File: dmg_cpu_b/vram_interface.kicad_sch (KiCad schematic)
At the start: 177 parts

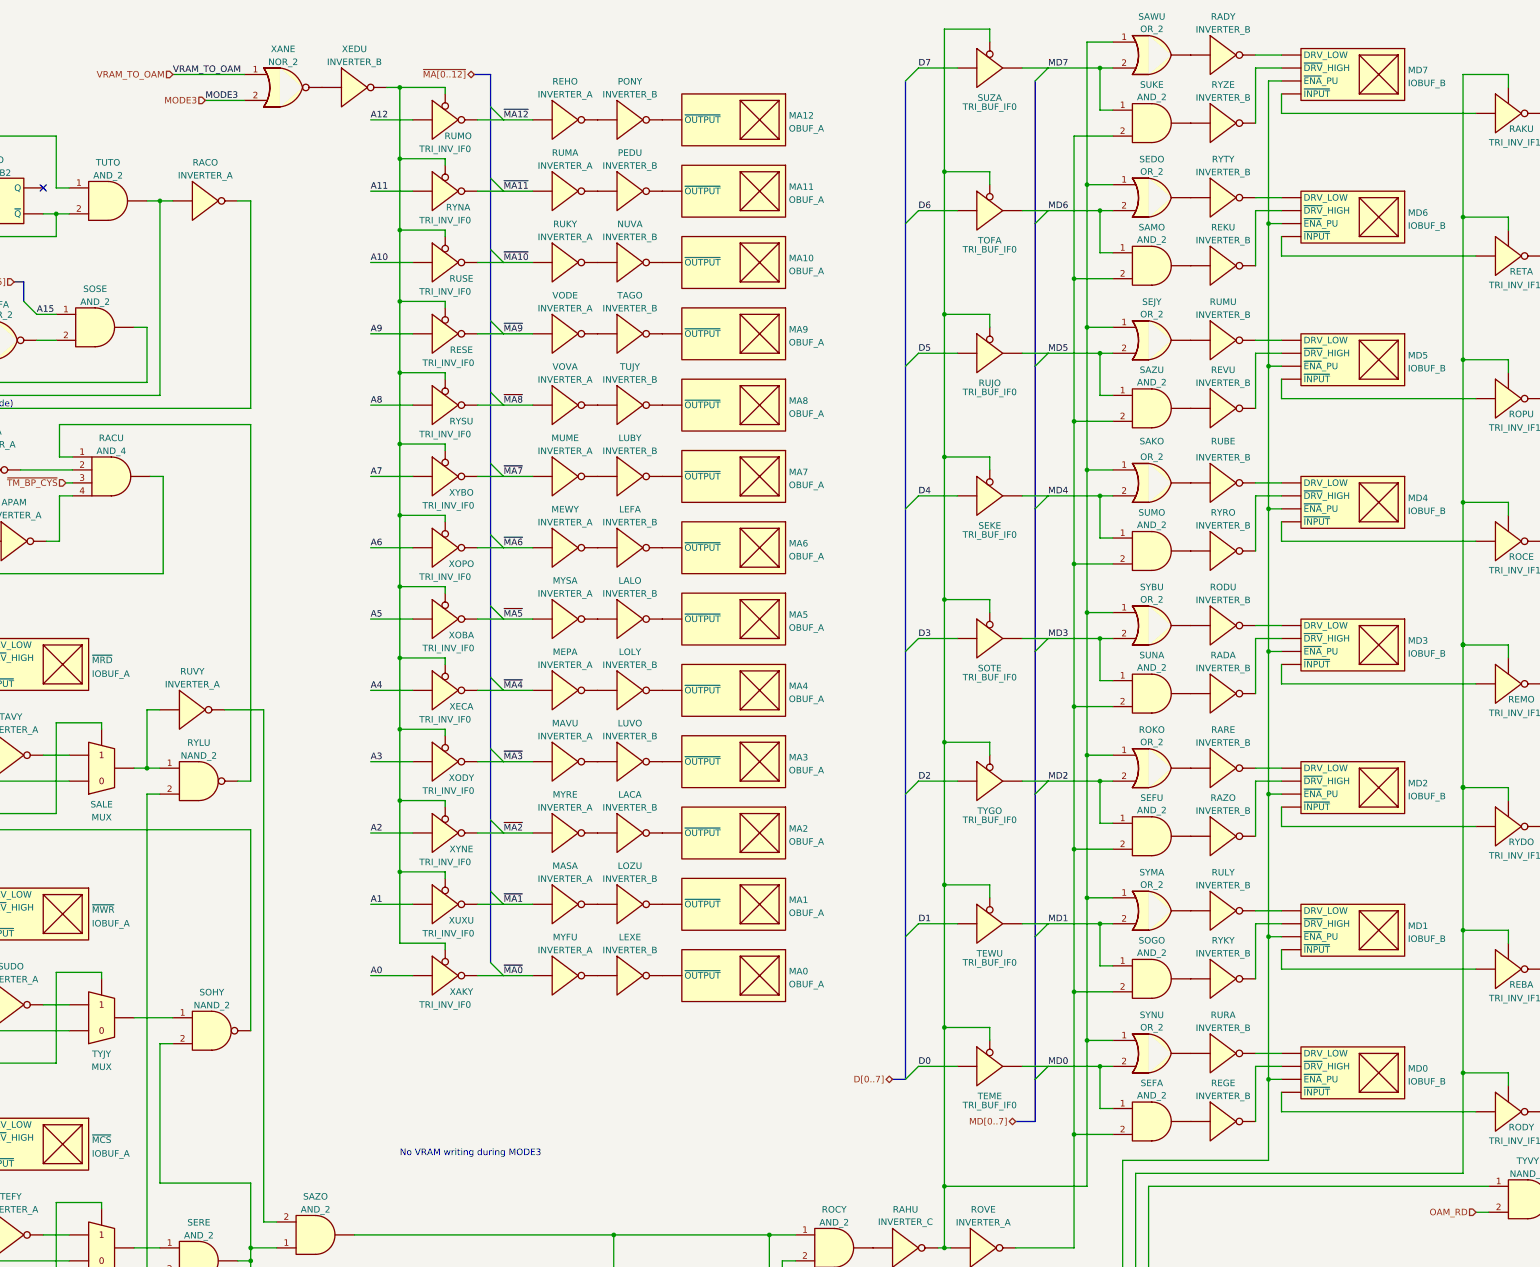
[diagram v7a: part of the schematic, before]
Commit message: Add pin numbers to IO pads in schematics
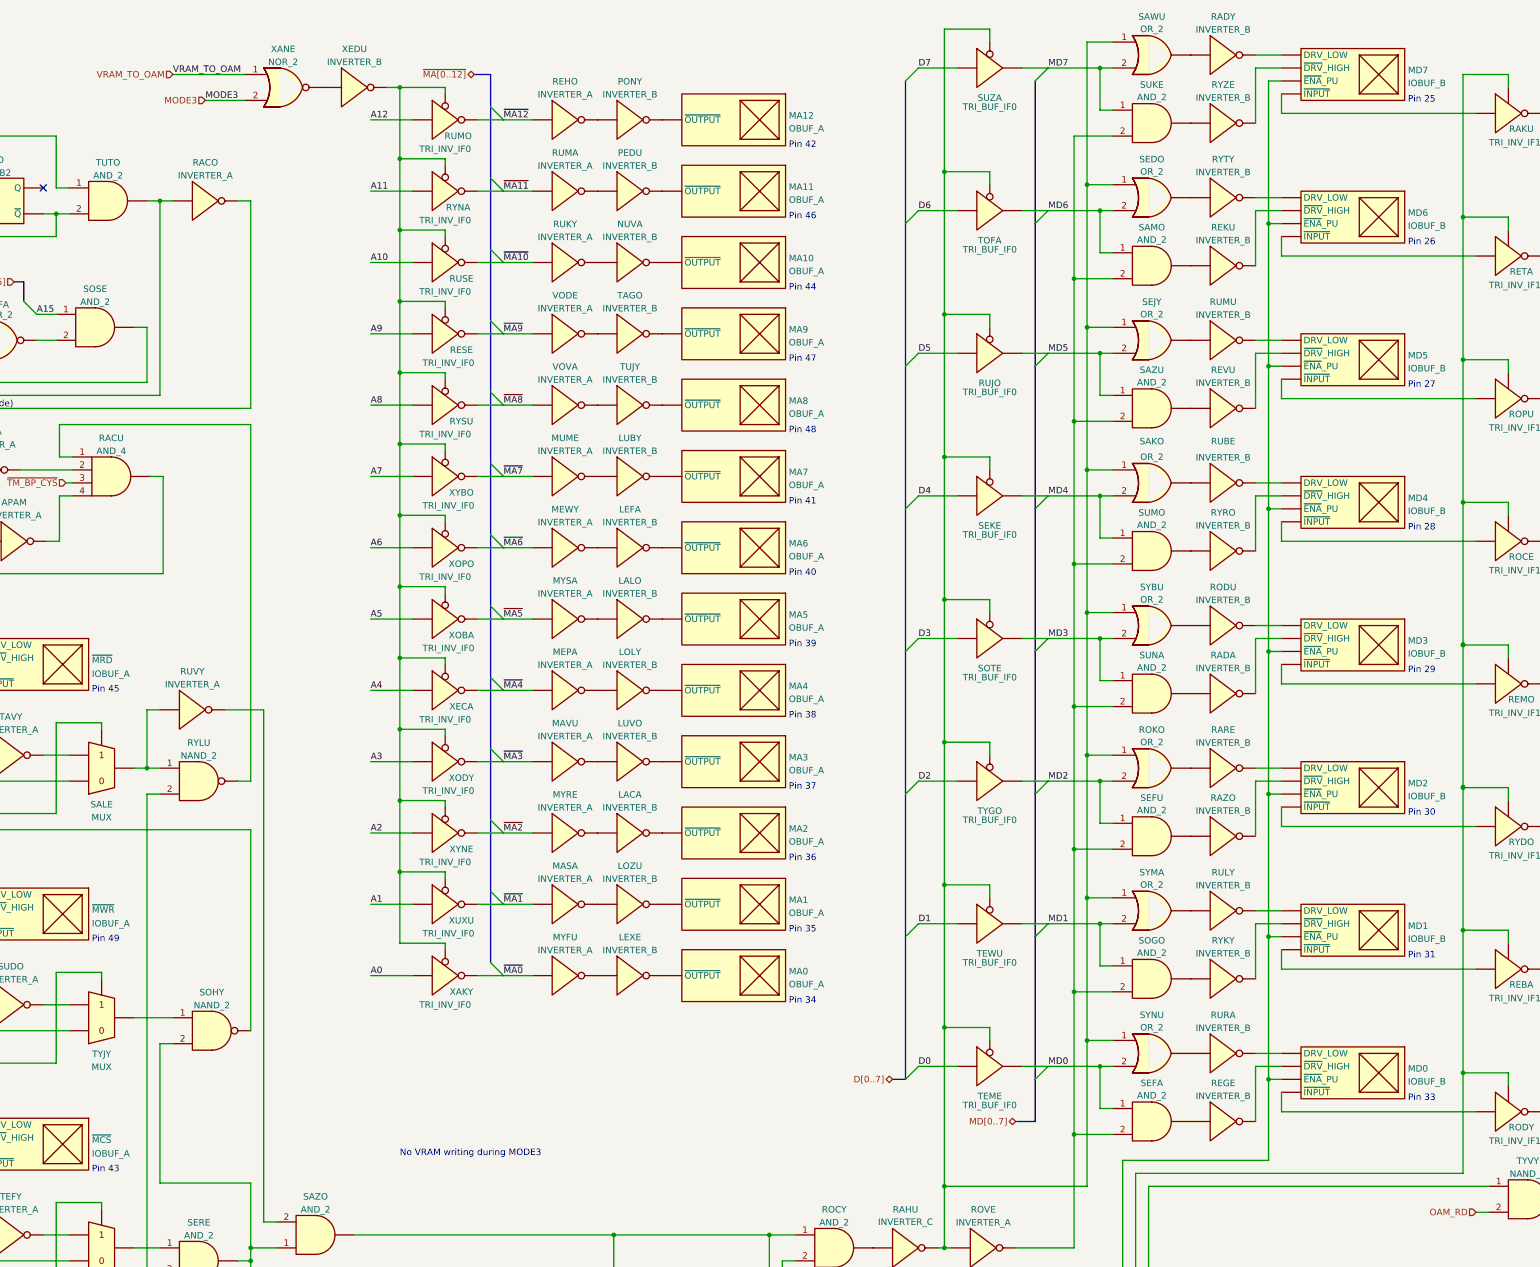
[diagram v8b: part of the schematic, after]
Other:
- note added: "Pin 25"
- note added: "Pin 26"
- note added: "Pin 27"
- note added: "Pin 28"
- note added: "Pin 29"
- note added: "Pin 30"
- note added: "Pin 31"
- note added: "Pin 33"
- note added: "Pin 34"
- note added: "Pin 35"
- note added: "Pin 36"
- note added: "Pin 37"
- note added: "Pin 38"
- note added: "Pin 39"
- note added: "Pin 40"
- note added: "Pin 41"
- note added: "Pin 42"
- note added: "Pin 43"
- note added: "Pin 44"
- note added: "Pin 45"
- note added: "Pin 46"
- note added: "Pin 47"
- note added: "Pin 48"
- note added: "Pin 49"
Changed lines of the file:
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@@
     (stroke (width 0) (type default) (color 0 0 0 0))
   )
+  (text "Pin 42" (at 219.075 40.64 0)
+    (effects (font (size 1.27 1.27)) (justify left bottom))
+  )
   (text "VRAM Address range 8000-9FFF" (at 18.415 86.36 0)
+    (effects (font (size 1.27 1.27)) (justify left bottom))
+  )
+  (text "Pin 39" (at 219.075 138.43 0)
+    (effects (font (size 1.27 1.27)) (justify left bottom))
+  )
+  (text "Pin 49" (at 82.55 196.215 0)
+    (effects (font (size 1.27 1.27)) (justify left bottom))
+  )
+  (text "Pin 40" (at 219.075 124.46 0)
+    (effects (font (size 1.27 1.27)) (justify left bottom))
+  )
+  (text "Pin 41" (at 219.075 110.49 0)
     (effects (font (size 1.27 1.27)) (justify left bottom))
   )
@@
     (effects (font (size 1.27 1.27)) (justify left bottom))
   )
+  (text "Pin 46" (at 219.075 54.61 0)
+    (effects (font (size 1.27 1.27)) (justify left bottom))
+  )
+  (text "Pin 25" (at 340.36 31.75 0)
+    (effects (font (size 1.27 1.27)) (justify left bottom))
+  )
   (text "No VRAM writing during MODE3" (at 142.875 238.125 0)
+    (effects (font (size 1.27 1.27)) (justify left bottom))
+  )
+  (text "Pin 33" (at 340.36 227.33 0)
+    (effects (font (size 1.27 1.27)) (justify left bottom))
+  )
+  (text "Pin 45" (at 82.55 147.32 0)
+    (effects (font (size 1.27 1.27)) (justify left bottom))
+  )
+  (text "Pin 43" (at 82.55 241.3 0)
+    (effects (font (size 1.27 1.27)) (justify left bottom))
+  )
+  (text "Pin 34" (at 219.075 208.28 0)
+    (effects (font (size 1.27 1.27)) (justify left bottom))
+  )
+  (text "Pin 48" (at 219.075 96.52 0)
+    (effects (font (size 1.27 1.27)) (justify left bottom))
+  )
+  (text "Pin 28" (at 340.36 115.57 0)
+    (effects (font (size 1.27 1.27)) (justify left bottom))
+  )
+  (text "Pin 31" (at 340.36 199.39 0)
+    (effects (font (size 1.27 1.27)) (justify left bottom))
+  )
+  (text "Pin 29" (at 340.36 143.51 0)
+    (effects (font (size 1.27 1.27)) (justify left bottom))
+  )
+  (text "Pin 36" (at 219.075 180.34 0)
+    (effects (font (size 1.27 1.27)) (justify left bottom))
+  )
+  (text "Pin 35" (at 219.075 194.31 0)
+    (effects (font (size 1.27 1.27)) (justify left bottom))
+  )
+  (text "Pin 47" (at 219.075 82.55 0)
+    (effects (font (size 1.27 1.27)) (justify left bottom))
+  )
+  (text "Pin 38" (at 219.075 152.4 0)
     (effects (font (size 1.27 1.27)) (justify left bottom))
   )
@@
     (effects (font (size 1.27 1.27)) (justify left bottom))
   )
+  (text "Pin 27" (at 340.36 87.63 0)
+    (effects (font (size 1.27 1.27)) (justify left bottom))
+  )
+  (text "Pin 30" (at 340.36 171.45 0)
+    (effects (font (size 1.27 1.27)) (justify left bottom))
+  )
+  (text "Pin 26" (at 340.36 59.69 0)
+    (effects (font (size 1.27 1.27)) (justify left bottom))
+  )
+  (text "Pin 37" (at 219.075 166.37 0)
+    (effects (font (size 1.27 1.27)) (justify left bottom))
+  )
+  (text "Pin 44" (at 219.075 68.58 0)
+    (effects (font (size 1.27 1.27)) (justify left bottom))
+  )
